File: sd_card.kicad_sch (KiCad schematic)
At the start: 2 parts, among them J2 Micro_SD_Card

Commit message: Assign footprints to symbols
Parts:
- J9: renamed from J2; footprint PUTM_Kicad_FOOTPRINTS:112K-TAA0-RA1 -> Local_Library:112K-TAA0-RA1
- renumbered C20 to C21
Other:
- moved on the sheet: C21, J9
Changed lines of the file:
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@@
     (title "SD Card")
     (date "2022-12-17")
-    (rev "0.1.0")
+    (rev "${REVISION}")
   )
-  (wire (pts (xy 176.53 116.84) (xy 175.26 116.84))
+  (wire (pts (xy 175.26 115.57) (xy 173.99 115.57))
     (stroke (width 0) (type default) (color 0 0 0 0))
   )
-  (wire (pts (xy 127 93.98) (xy 132.08 93.98))
+  (wire (pts (xy 125.73 92.71) (xy 130.81 92.71))
     (stroke (width 0) (type default) (color 0 0 0 0))
   )
-  (wire (pts (xy 132.08 111.76) (xy 127 111.76))
+  (wire (pts (xy 130.81 110.49) (xy 125.73 110.49))
     (stroke (width 0) (type default) (color 0 0 0 0))
   )
-  (wire (pts (xy 127 104.14) (xy 132.08 104.14))
+  (wire (pts (xy 125.73 102.87) (xy 130.81 102.87))
     (stroke (width 0) (type default) (color 0 0 0 0))
   )
-  (wire (pts (xy 129.54 106.68) (xy 132.08 106.68))
+  (wire (pts (xy 128.27 105.41) (xy 130.81 105.41))
     (stroke (width 0) (type default) (color 0 0 0 0))
   )
-  (wire (pts (xy 190.5 104.14) (xy 190.5 106.68))
+  (wire (pts (xy 190.5 102.87) (xy 190.5 105.41))
     (stroke (width 0) (type default) (color 0 0 0 0))
   )
-  (wire (pts (xy 176.53 118.11) (xy 176.53 116.84))
+  (wire (pts (xy 175.26 116.84) (xy 175.26 115.57))
     (stroke (width 0) (type default) (color 0 0 0 0))
   )
-  (wire (pts (xy 127 96.52) (xy 132.08 96.52))
+  (wire (pts (xy 125.73 95.25) (xy 130.81 95.25))
     (stroke (width 0) (type default) (color 0 0 0 0))
   )
-  (wire (pts (xy 127 109.22) (xy 132.08 109.22))
+  (wire (pts (xy 125.73 107.95) (xy 130.81 107.95))
     (stroke (width 0) (type default) (color 0 0 0 0))
   )
-  (wire (pts (xy 190.5 97.79) (xy 190.5 99.06))
+  (wire (pts (xy 190.5 96.52) (xy 190.5 97.79))
     (stroke (width 0) (type default) (color 0 0 0 0))
   )
-  (wire (pts (xy 132.08 101.6) (xy 129.54 101.6))
+  (wire (pts (xy 130.81 100.33) (xy 128.27 100.33))
     (stroke (width 0) (type default) (color 0 0 0 0))
   )
-  (wire (pts (xy 129.54 114.3) (xy 129.54 106.68))
+  (wire (pts (xy 128.27 113.03) (xy 128.27 105.41))
     (stroke (width 0) (type default) (color 0 0 0 0))
   )
-  (wire (pts (xy 129.54 91.44) (xy 129.54 101.6))
+  (wire (pts (xy 128.27 90.17) (xy 128.27 100.33))
     (stroke (width 0) (type default) (color 0 0 0 0))
   )
-  (wire (pts (xy 127 99.06) (xy 132.08 99.06))
+  (wire (pts (xy 125.73 97.79) (xy 130.81 97.79))
     (stroke (width 0) (type default) (color 0 0 0 0))
   )
-  (hierarchical_label "SDMMC_D3" (shape bidirectional) (at 127 96.52 180)
+  (hierarchical_label "SDMMC_D3" (shape bidirectional) (at 125.73 95.25 180)
     (effects (font (size 1.27 1.27)) (justify right))
   )
-  (hierarchical_label "SDMMC_D1" (shape bidirectional) (at 127 111.76 180)
+  (hierarchical_label "SDMMC_D1" (shape bidirectional) (at 125.73 110.49 180)
     (effects (font (size 1.27 1.27)) (justify right))
   )
-  (hierarchical_label "SDMMC_D2" (shape bidirectional) (at 127 93.98 180)
+  (hierarchical_label "SDMMC_D2" (shape bidirectional) (at 125.73 92.71 180)
     (effects (font (size 1.27 1.27)) (justify right))
   )
-  (hierarchical_label "SDMMC_D0" (shape bidirectional) (at 127 109.22 180)
+  (hierarchical_label "SDMMC_D0" (shape bidirectional) (at 125.73 107.95 180)
     (effects (font (size 1.27 1.27)) (justify right))
   )
-  (hierarchical_label "SDMMC_CLK" (shape input) (at 127 104.14 180)
+  (hierarchical_label "SDMMC_CLK" (shape input) (at 125.73 102.87 180)
     (effects (font (size 1.27 1.27)) (justify right))
   )
-  (hierarchical_label "SDMMC_CMD" (shape input) (at 127 99.06 180)
+  (hierarchical_label "SDMMC_CMD" (shape input) (at 125.73 97.79 180)
     (effects (font (size 1.27 1.27)) (justify right))
   )
-  (symbol (lib_id "Connector:Micro_SD_Card") (at 154.94 101.6 0) (unit 1)
+  (symbol (lib_id "Connector:Micro_SD_Card") (at 153.67 100.33 0) (unit 1)
     (in_bom yes) (on_board yes)
-    (property "Reference" "J2" (id 0) (at 153.67 85.9282 0))
-    (property "Value" "Micro_SD_Card" (id 1) (at 153.67 85.6996 0)
+    (property "Reference" "J9" (id 0) (at 152.4 84.6582 0))
+    (property "Value" "Micro_SD_Card" (id 1) (at 152.4 84.4296 0)
       (effects (font (size 1.27 1.27)) hide)
     )
-    (property "Footprint" "PUTM_Kicad_FOOTPRINTS:112K-TAA0-RA1" (id 2) (at 184.15 93.98 0)
+    (property "Footprint" "Local_Library:112K-TAA0-RA1" (id 2) (at 182.88 92.71 0)
       (effects (font (size 1.27 1.27)) hide)
     )
-    (property "Datasheet" "https://www.tme.eu/Document/c3b9a7ded342d5553aff6a91c42e4fab/112K-TAA0-RA1.pdf" (id 3) (at 154.94 101.6 0)
+    (property "Datasheet" "https://www.tme.eu/Document/c3b9a7ded342d5553aff6a91c42e4fab/112K-TAA0-RA1.pdf" (id 3) (at 153.67 100.33 0)
       (effects (font (size 1.27 1.27)) hide)
     )
@@
     (pin "9")
   )
-  (symbol (lib_id "Device:C_Small") (at 190.5 101.6 0) (unit 1)
+  (symbol (lib_id "Device:C_Small") (at 190.5 100.33 0) (unit 1)
     (in_bom yes) (on_board yes)
-    (property "Reference" "C20" (id 0) (at 192.8368 100.4316 0)
+    (property "Reference" "C21" (id 0) (at 192.8368 99.1616 0)
       (effects (font (size 1.27 1.27)) (justify left))
     )
-    (property "Value" "4.7μF" (id 1) (at 192.8368 102.743 0)
+    (property "Value" "4.7μF" (id 1) (at 192.8368 101.473 0)
       (effects (font (size 1.27 1.27)) (justify left))
     )
-    (property "Footprint" "Capacitor_SMD:C_0603_1608Metric" (id 2) (at 190.5 101.6 0)
+    (property "Footprint" "Capacitor_SMD:C_0603_1608Metric" (id 2) (at 190.5 100.33 0)
       (effects (font (size 1.27 1.27)) hide)
     )
-    (property "Datasheet" "~" (id 3) (at 190.5 101.6 0)
+    (property "Datasheet" "~" (id 3) (at 190.5 100.33 0)
       (effects (font (size 1.27 1.27)) hide)
     )
-    (property "LCSC" "C19666" (id 4) (at 190.5 101.6 0)
+    (property "LCSC" "C19666" (id 4) (at 190.5 100.33 0)
       (effects (font (size 1.27 1.27)) hide)
     )
@@
     (pin "2")
   )
-  (symbol (lib_id "power:GND") (at 190.5 106.68 0) (unit 1)
+  (symbol (lib_id "power:GND") (at 190.5 105.41 0) (unit 1)
     (in_bom yes) (on_board yes)
-    (property "Reference" "#PWR040" (id 0) (at 190.5 113.03 0)
+    (property "Reference" "#PWR053" (id 0) (at 190.5 111.76 0)
       (effects (font (size 1.27 1.27)) hide)
     )
-    (property "Value" "GND" (id 1) (at 190.627 111.0742 0))
-    (property "Footprint" "" (id 2) (at 190.5 106.68 0)
+    (property "Value" "GND" (id 1) (at 190.627 109.8042 0))
+    (property "Footprint" "" (id 2) (at 190.5 105.41 0)
       (effects (font (size 1.27 1.27)) hide)
     )
-    (property "Datasheet" "" (id 3) (at 190.5 106.68 0)
+    (property "Datasheet" "" (id 3) (at 190.5 105.41 0)
       (effects (font (size 1.27 1.27)) hide)
     )
     (pin "1")
   )
-  (symbol (lib_id "power:+3.3V") (at 190.5 97.79 0) (unit 1)
+  (symbol (lib_id "power:+3.3V") (at 190.5 96.52 0) (unit 1)
     (in_bom yes) (on_board yes) (fields_autoplaced)
-    (property "Reference" "#PWR039" (id 0) (at 190.5 101.6 0)
+    (property "Reference" "#PWR052" (id 0) (at 190.5 100.33 0)
       (effects (font (size 1.27 1.27)) hide)
     )
-    (property "Value" "+3.3V" (id 1) (at 190.5 92.71 0))
-    (property "Footprint" "" (id 2) (at 190.5 97.79 0)
+    (property "Value" "+3.3V" (id 1) (at 190.5 91.44 0))
+    (property "Footprint" "" (id 2) (at 190.5 96.52 0)
       (effects (font (size 1.27 1.27)) hide)
     )
-    (property "Datasheet" "" (id 3) (at 190.5 97.79 0)
+    (property "Datasheet" "" (id 3) (at 190.5 96.52 0)
       (effects (font (size 1.27 1.27)) hide)
     )
     (pin "1")
   )
-  (symbol (lib_id "power:+3.3V") (at 129.54 91.44 0) (unit 1)
+  (symbol (lib_id "power:+3.3V") (at 128.27 90.17 0) (unit 1)
     (in_bom yes) (on_board yes) (fields_autoplaced)
-    (property "Reference" "#PWR038" (id 0) (at 129.54 95.25 0)
+    (property "Reference" "#PWR051" (id 0) (at 128.27 93.98 0)
       (effects (font (size 1.27 1.27)) hide)
     )
-    (property "Value" "+3.3V" (id 1) (at 129.54 86.36 0))
-    (property "Footprint" "" (id 2) (at 129.54 91.44 0)
+    (property "Value" "+3.3V" (id 1) (at 128.27 85.09 0))
+    (property "Footprint" "" (id 2) (at 128.27 90.17 0)
       (effects (font (size 1.27 1.27)) hide)
     )
-    (property "Datasheet" "" (id 3) (at 129.54 91.44 0)
+    (property "Datasheet" "" (id 3) (at 128.27 90.17 0)
       (effects (font (size 1.27 1.27)) hide)
     )
     (pin "1")
   )
-  (symbol (lib_id "power:GND") (at 129.54 114.3 0) (unit 1)
+  (symbol (lib_id "power:GND") (at 128.27 113.03 0) (unit 1)
     (in_bom yes) (on_board yes)
-    (property "Reference" "#PWR041" (id 0) (at 129.54 120.65 0)
+    (property "Reference" "#PWR054" (id 0) (at 128.27 119.38 0)
       (effects (font (size 1.27 1.27)) hide)
     )
-    (property "Value" "GND" (id 1) (at 129.667 118.6942 0))
-    (property "Footprint" "" (id 2) (at 129.54 114.3 0)
+    (property "Value" "GND" (id 1) (at 128.397 117.4242 0))
+    (property "Footprint" "" (id 2) (at 128.27 113.03 0)
       (effects (font (size 1.27 1.27)) hide)
     )
-    (property "Datasheet" "" (id 3) (at 129.54 114.3 0)
+    (property "Datasheet" "" (id 3) (at 128.27 113.03 0)
       (effects (font (size 1.27 1.27)) hide)
     )
     (pin "1")
   )
-  (symbol (lib_id "power:GND") (at 176.53 118.11 0) (unit 1)
+  (symbol (lib_id "power:GND") (at 175.26 116.84 0) (unit 1)
     (in_bom yes) (on_board yes)
-    (property "Reference" "#PWR042" (id 0) (at 176.53 124.46 0)
+    (property "Reference" "#PWR055" (id 0) (at 175.26 123.19 0)
       (effects (font (size 1.27 1.27)) hide)
     )
-    (property "Value" "GND" (id 1) (at 176.657 122.5042 0))
-    (property "Footprint" "" (id 2) (at 176.53 118.11 0)
+    (property "Value" "GND" (id 1) (at 175.387 121.2342 0))
+    (property "Footprint" "" (id 2) (at 175.26 116.84 0)
       (effects (font (size 1.27 1.27)) hide)
     )
-    (property "Datasheet" "" (id 3) (at 176.53 118.11 0)
+    (property "Datasheet" "" (id 3) (at 175.26 116.84 0)
       (effects (font (size 1.27 1.27)) hide)
     )

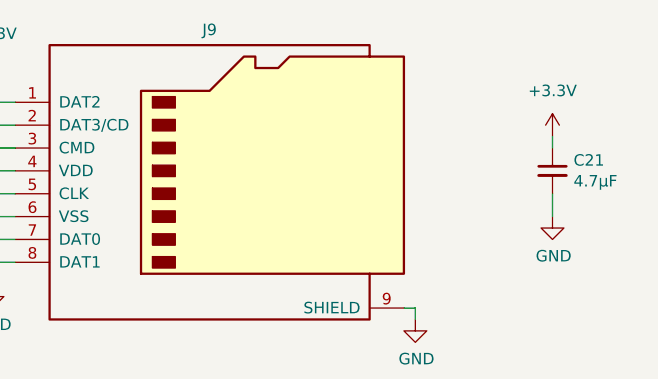
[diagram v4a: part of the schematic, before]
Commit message: Use single connector for I/O
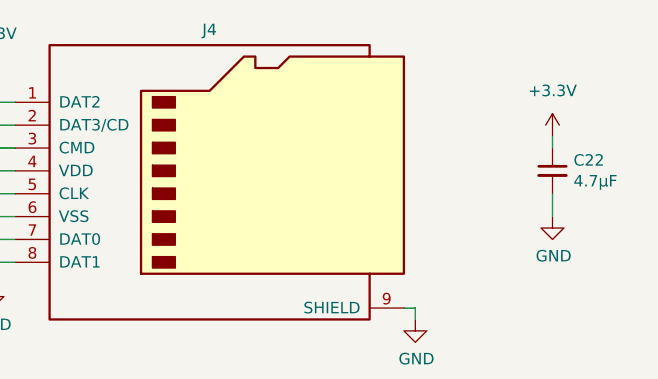
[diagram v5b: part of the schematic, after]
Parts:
- renumbered C21 to C22, J9 to J4
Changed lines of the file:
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@@
   (title_block
     (title "SD Card")
-    (date "2022-12-17")
+    (date "2022-12-20")
     (rev "${REVISION}")
   )
@@
   (symbol (lib_id "Connector:Micro_SD_Card") (at 153.67 100.33 0) (unit 1)
     (in_bom yes) (on_board yes)
-    (property "Reference" "J9" (id 0) (at 152.4 84.6582 0))
+    (property "Reference" "J4" (id 0) (at 152.4 84.6582 0))
     (property "Value" "Micro_SD_Card" (id 1) (at 152.4 84.4296 0)
       (effects (font (size 1.27 1.27)) hide)
@@
   (symbol (lib_id "Device:C_Small") (at 190.5 100.33 0) (unit 1)
     (in_bom yes) (on_board yes)
-    (property "Reference" "C21" (id 0) (at 192.8368 99.1616 0)
+    (property "Reference" "C22" (id 0) (at 192.8368 99.1616 0)
       (effects (font (size 1.27 1.27)) (justify left))
     )
@@
   (symbol (lib_id "power:GND") (at 190.5 105.41 0) (unit 1)
     (in_bom yes) (on_board yes)
-    (property "Reference" "#PWR053" (id 0) (at 190.5 111.76 0)
+    (property "Reference" "#PWR051" (id 0) (at 190.5 111.76 0)
       (effects (font (size 1.27 1.27)) hide)
     )
@@
   (symbol (lib_id "power:+3.3V") (at 190.5 96.52 0) (unit 1)
     (in_bom yes) (on_board yes) (fields_autoplaced)
-    (property "Reference" "#PWR052" (id 0) (at 190.5 100.33 0)
+    (property "Reference" "#PWR050" (id 0) (at 190.5 100.33 0)
       (effects (font (size 1.27 1.27)) hide)
     )
@@
   (symbol (lib_id "power:+3.3V") (at 128.27 90.17 0) (unit 1)
     (in_bom yes) (on_board yes) (fields_autoplaced)
-    (property "Reference" "#PWR051" (id 0) (at 128.27 93.98 0)
+    (property "Reference" "#PWR049" (id 0) (at 128.27 93.98 0)
       (effects (font (size 1.27 1.27)) hide)
     )
@@
   (symbol (lib_id "power:GND") (at 128.27 113.03 0) (unit 1)
     (in_bom yes) (on_board yes)
-    (property "Reference" "#PWR054" (id 0) (at 128.27 119.38 0)
+    (property "Reference" "#PWR052" (id 0) (at 128.27 119.38 0)
       (effects (font (size 1.27 1.27)) hide)
     )
@@
   (symbol (lib_id "power:GND") (at 175.26 116.84 0) (unit 1)
     (in_bom yes) (on_board yes)
-    (property "Reference" "#PWR055" (id 0) (at 175.26 123.19 0)
+    (property "Reference" "#PWR053" (id 0) (at 175.26 123.19 0)
       (effects (font (size 1.27 1.27)) hide)
     )

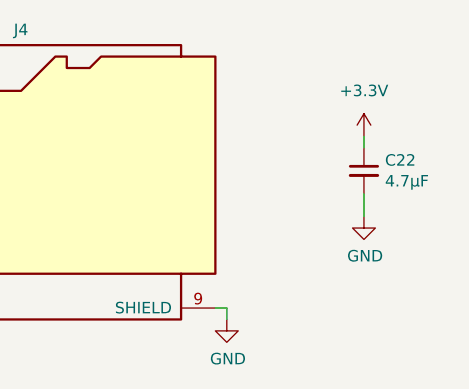
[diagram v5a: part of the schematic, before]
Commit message: Remove 5V LDO regulator
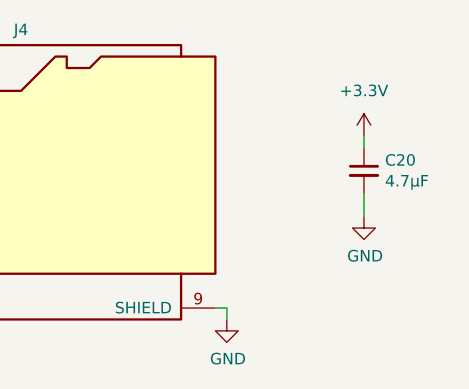
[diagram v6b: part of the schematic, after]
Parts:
- renumbered C22 to C20
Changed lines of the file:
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@@
   (symbol (lib_id "Device:C_Small") (at 190.5 100.33 0) (unit 1)
     (in_bom yes) (on_board yes)
-    (property "Reference" "C22" (id 0) (at 192.8368 99.1616 0)
+    (property "Reference" "C20" (id 0) (at 192.8368 99.1616 0)
       (effects (font (size 1.27 1.27)) (justify left))
     )
@@
   (symbol (lib_id "power:GND") (at 190.5 105.41 0) (unit 1)
     (in_bom yes) (on_board yes)
-    (property "Reference" "#PWR051" (id 0) (at 190.5 111.76 0)
+    (property "Reference" "#PWR050" (id 0) (at 190.5 111.76 0)
       (effects (font (size 1.27 1.27)) hide)
     )
@@
   (symbol (lib_id "power:+3.3V") (at 190.5 96.52 0) (unit 1)
     (in_bom yes) (on_board yes) (fields_autoplaced)
-    (property "Reference" "#PWR050" (id 0) (at 190.5 100.33 0)
+    (property "Reference" "#PWR049" (id 0) (at 190.5 100.33 0)
       (effects (font (size 1.27 1.27)) hide)
     )
@@
   (symbol (lib_id "power:+3.3V") (at 128.27 90.17 0) (unit 1)
     (in_bom yes) (on_board yes) (fields_autoplaced)
-    (property "Reference" "#PWR049" (id 0) (at 128.27 93.98 0)
+    (property "Reference" "#PWR048" (id 0) (at 128.27 93.98 0)
       (effects (font (size 1.27 1.27)) hide)
     )
@@
   (symbol (lib_id "power:GND") (at 128.27 113.03 0) (unit 1)
     (in_bom yes) (on_board yes)
-    (property "Reference" "#PWR052" (id 0) (at 128.27 119.38 0)
+    (property "Reference" "#PWR051" (id 0) (at 128.27 119.38 0)
       (effects (font (size 1.27 1.27)) hide)
     )
@@
   (symbol (lib_id "power:GND") (at 175.26 116.84 0) (unit 1)
     (in_bom yes) (on_board yes)
-    (property "Reference" "#PWR053" (id 0) (at 175.26 123.19 0)
+    (property "Reference" "#PWR052" (id 0) (at 175.26 123.19 0)
       (effects (font (size 1.27 1.27)) hide)
     )

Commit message: Arrange footprints
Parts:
- removed C20: 4.7μF, Capacitor_SMD:C_0603_1608Metric, symbol Device:C_Small
- added C21: 4.7μF, Capacitor_Tantalum_SMD:CP_EIA-3216-10_Kemet-I, symbol Device:C_Polarized_Small
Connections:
- net +3.3V: now also C21.1
- net GND: now also C21.2
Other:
- company: (none) -> Authors: H. Fedarovich, I. Kajdan
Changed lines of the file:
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@@
   (title_block
     (title "SD Card")
-    (date "2022-12-20")
+    (date "2022-12-23")
     (rev "${REVISION}")
+    (company "Authors: H. Fedarovich, I. Kajdan")
+    (comment 1 "Reviewer: A. Bondyra")
   )
   (wire (pts (xy 175.26 115.57) (xy 173.99 115.57))
@@
     (stroke (width 0) (type default) (color 0 0 0 0))
   )
-  (wire (pts (xy 190.5 96.52) (xy 190.5 97.79))
+  (wire (pts (xy 130.81 100.33) (xy 128.27 100.33))
     (stroke (width 0) (type default) (color 0 0 0 0))
   )
-  (wire (pts (xy 130.81 100.33) (xy 128.27 100.33))
+  (wire (pts (xy 190.5 96.52) (xy 190.5 97.79))
     (stroke (width 0) (type default) (color 0 0 0 0))
   )
@@
     (pin "9")
   )
-  (symbol (lib_id "Device:C_Small") (at 190.5 100.33 0) (unit 1)
-    (in_bom yes) (on_board yes)
-    (property "Reference" "C20" (id 0) (at 192.8368 99.1616 0)
+  (symbol (lib_id "Device:C_Polarized_Small") (at 190.5 100.33 0) (unit 1)
+    (in_bom yes) (on_board yes) (fields_autoplaced)
+    (property "Reference" "C21" (id 0) (at 193.04 98.5138 0)
       (effects (font (size 1.27 1.27)) (justify left))
     )
-    (property "Value" "4.7μF" (id 1) (at 192.8368 101.473 0)
+    (property "Value" "4.7μF" (id 1) (at 193.04 101.0538 0)
       (effects (font (size 1.27 1.27)) (justify left))
     )
-    (property "Footprint" "Capacitor_SMD:C_0603_1608Metric" (id 2) (at 190.5 100.33 0)
+    (property "Footprint" "Capacitor_Tantalum_SMD:CP_EIA-3216-10_Kemet-I" (id 2) (at 190.5 100.33 0)
       (effects (font (size 1.27 1.27)) hide)
     )
     (property "Datasheet" "~" (id 3) (at 190.5 100.33 0)
-      (effects (font (size 1.27 1.27)) hide)
-    )
-    (property "LCSC" "C19666" (id 4) (at 190.5 100.33 0)
       (effects (font (size 1.27 1.27)) hide)
     )
@@
   (symbol (lib_id "power:GND") (at 190.5 105.41 0) (unit 1)
     (in_bom yes) (on_board yes)
-    (property "Reference" "#PWR050" (id 0) (at 190.5 111.76 0)
+    (property "Reference" "#PWR051" (id 0) (at 190.5 111.76 0)
       (effects (font (size 1.27 1.27)) hide)
     )
@@
   (symbol (lib_id "power:+3.3V") (at 190.5 96.52 0) (unit 1)
     (in_bom yes) (on_board yes) (fields_autoplaced)
-    (property "Reference" "#PWR049" (id 0) (at 190.5 100.33 0)
+    (property "Reference" "#PWR050" (id 0) (at 190.5 100.33 0)
       (effects (font (size 1.27 1.27)) hide)
     )
@@
   (symbol (lib_id "power:+3.3V") (at 128.27 90.17 0) (unit 1)
     (in_bom yes) (on_board yes) (fields_autoplaced)
-    (property "Reference" "#PWR048" (id 0) (at 128.27 93.98 0)
+    (property "Reference" "#PWR049" (id 0) (at 128.27 93.98 0)
       (effects (font (size 1.27 1.27)) hide)
     )
@@
   (symbol (lib_id "power:GND") (at 128.27 113.03 0) (unit 1)
     (in_bom yes) (on_board yes)
-    (property "Reference" "#PWR051" (id 0) (at 128.27 119.38 0)
+    (property "Reference" "#PWR052" (id 0) (at 128.27 119.38 0)
       (effects (font (size 1.27 1.27)) hide)
     )
@@
   (symbol (lib_id "power:GND") (at 175.26 116.84 0) (unit 1)
     (in_bom yes) (on_board yes)
-    (property "Reference" "#PWR052" (id 0) (at 175.26 123.19 0)
+    (property "Reference" "#PWR053" (id 0) (at 175.26 123.19 0)
       (effects (font (size 1.27 1.27)) hide)
     )
